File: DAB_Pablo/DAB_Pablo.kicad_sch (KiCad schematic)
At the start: 27 parts, among them U1 UCC21710QDWQ1

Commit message: Se completa Primary Side Half-Bridge 1
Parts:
- added C155, C157, C325, C326: 10uF/50V, Capacitor_SMD:C_1206_3216Metric, symbol Device:C
- added C156, C158: 0.1uF/50V, Capacitor_SMD:C_0201_0603Metric, symbol Device:C
- added C159, C160, C165, C167: 100nF, Capacitor_SMD:C_0201_0603Metric, symbol Device:C
- added C161, C162, C163, C164: 330pF, Capacitor_SMD:C_0201_0603Metric, symbol Device:C
- added C166, C168: 2.2uF/50V, Capacitor_SMD:C_1206_3216Metric, symbol Device:C
- added C171, C176, C181: 0.1uF/50V, Capacitor_SMD:C_1206_3216Metric, symbol Device:C
- added C172: 3.3uF/50V, Capacitor_SMD:C_1206_3216Metric, symbol Device:C
- added C177: 1uF/100V, Capacitor_SMD:C_1206_3216Metric, symbol Device:C
- added C180, C184, C190, C191, C192: 100pF/50V, Capacitor_SMD:C_0201_0603Metric, symbol Device:C
- added C182: 0.47uF/50V, Capacitor_SMD:C_1206_3216Metric, symbol Device:C
- added C189: 330pF/50V, Capacitor_SMD:C_0201_0603Metric, symbol Device:C
- added D15: 1200 V 1A, Diode_SMD:D_SMA, symbol Device:D
- added D17, D20: LED, LED_SMD:LED_0201_0603Metric, symbol Device:LED
- added R144, R150: 0, Resistor_SMD:R_0201_0603Metric, symbol Device:R
- added R154: 15k, Resistor_SMD:R_0201_0603Metric, symbol Device:R
- added R155: 18k, Resistor_SMD:R_0201_0603Metric, symbol Device:R
- added R171: 2k, Resistor_SMD:R_0201_0603Metric, symbol Device:R
- added R183, R4: 1.0k, Resistor_SMD:R_0201_0603Metric, symbol Device:R
- added R185, R187: 100k, Resistor_SMD:R_0201_0603Metric, symbol Device:R
- added R186, R190, R24, R25: 10k, Resistor_SMD:R_0201_0603Metric, symbol Device:R
- added R188, R191: 107k, Resistor_SMD:R_0201_0603Metric, symbol Device:R
- added R189, R192: 30k, Resistor_SMD:R_0201_0603Metric, symbol Device:R
- added R196, R198: 16.2k, Resistor_SMD:R_0201_0603Metric, symbol Device:R
- added R197, R199: 49.9k, Resistor_SMD:R_0201_0603Metric, symbol Device:R
- added R201, R203, R214: 100, Resistor_SMD:R_0201_0603Metric, symbol Device:R
- added R215, R218: 2, Resistor_SMD:R_1206_3216Metric, symbol Device:R
- added R90, R93: 3.6k, Resistor_SMD:R_0201_0603Metric, symbol Device:R
- added U14, U24: UCC14141QDWNRQ1, SSOP36_DWN_TEX, symbol UCC14141QDWNRQ1:UCC14141QDWNRQ1
- added U30: UCC21710QDWQ1, SOIC16_DW_TEX, symbol UCC21710:UCC21710QDWQ1
- renumbered U1 to U29
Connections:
- net +15V_TOP1: now also C165.2, C166.2, C167.2, C168.2, R154.2, R188.2, R191.2, R24.2, R25.2, U14.28 (VDD), U14.29 (VDD), U24.28 (VDD), U24.29 (VDD), U30.5 (VDD)
- net -4V_TOP1: now also C161.1, C162.1, C163.1, C164.1, C165.1, C166.1, C167.1, C168.1, D17.1 (K), D20.1 (K), R196.1, R197.1, R198.1, R199.1, U14.19 (VEE), U14.20 (VEE), U14.21 (VEE), U14.22 (VEE), U14.23 (VEE), U14.24 (VEE), U14.25 (VEE), U14.26 (VEE), U14.27 (VEE), U14.30 (VEE), U14.31 (VEE), U14.35 (VEEA), U14.36 (VEE), U24.19 (VEE), U24.20 (VEE), U24.21 (VEE), U24.22 (VEE), U24.23 (VEE), U24.24 (VEE), U24.25 (VEE), U24.26 (VEE), U24.27 (VEE), U24.30 (VEE), U24.31 (VEE), U24.35 (VEEA), U24.36 (VEE)
- net GND1: now also C155.1, C156.1, C157.1, C158.1, C159.1, C160.1, C180.1, C184.1, C190.1, C191.1, C192.1, C325.1, C326.1, R90.1, R93.1, U14.1 (GNDP), U14.10 (GNDP), U14.11 (GNDP), U14.12 (GNDP), U14.13 (GNDP), U14.14 (GNDP), U14.15 (GNDP), U14.16 (GNDP), U14.17 (GNDP), U14.18 (GNDP), U14.2 (GNDP), U14.5 (GNDP), U14.8 (GNDP), U14.9 (GNDP), U24.1 (GNDP), U24.10 (GNDP), U24.11 (GNDP), U24.12 (GNDP), U24.13 (GNDP), U24.14 (GNDP), U24.15 (GNDP), U24.16 (GNDP), U24.17 (GNDP), U24.18 (GNDP), U24.2 (GNDP), U24.5 (GNDP), U24.8 (GNDP), U24.9 (GNDP), U30.9 (GND)
- net GND_TOP1: now also C189.1, R171.1, R183.1, R189.2, R192.2, R4.1
- net PWM1A_1: now also R201.1
- net PWM1B_1: now also R203.1
- net RDY: now also R144.1
- net TMP_HB1_P: now also U30.16 (APWM)
- net /DESAT_PRI: now also R150.1
- net /RST: now also R214.1
- net -3V3_D renamed 3V3_D
- net 3V3_D: now also C191.2, C192.2, R185.1, R187.1, U30.15 (VCC)
- new net: C189.2, R155.1, R171.2, U30.2 (OC)
- new net: C161.2, R188.1, R196.2, U14.34 (FBVDD)
- new net: R185.2, U14.3 (*PG)
- new net: R183.2, U14.32 (RLIM)
- new net: C162.2, R189.1, R197.2, U14.33 (FBVEE)
- new net: C159.2, R186.1, R90.2, U14.4 (ENA)
- new net: C164.2, R192.1, R199.2, U24.33 (FBVEE)
- new net: C184.2, R203.2, U30.11 (IN-)
- new net: R144.2, U30.12 (RDY)
- new net: C160.2, R190.1, R93.2, U24.4 (ENA)
- new net: C190.2, R214.2, U30.14 (*RST/EN)
- new net: C163.2, R191.1, R198.2, U24.34 (FBVDD)
- new net: R187.2, U24.3 (*PG)
- new net: R4.2, U24.32 (RLIM)
- new net: D15.2 (A), R154.1, R155.2
- new net: D17.2 (A), R24.1
- new net: C180.2, R201.2, U30.10 (IN+)
- new net: R150.2, U30.13 (*FLT)
- new net: R218.1, U30.4 (OUTH)
- new net: R215.1, U30.6 (OUTL)
- new net: D20.2 (A), R25.1
- new net +15V_BOT1: C176.1, C177.1, C181.1, C182.1
- new net -4V_BOT1: C171.2, C172.2, C176.2, C177.2, U30.8 (VEE)
- new net 12V: C155.2, C156.2, C157.2, C158.2, C325.2, C326.2, R186.2, R190.2, U14.6 (VIN), U14.7 (VIN), U24.6 (VIN), U24.7 (VIN)
- new net D1L_P: D15.1 (K)
- new net G1L_P: R215.2, R218.2, U30.7 (CLMPI)
- new net GND_BOT1: C171.1, C172.1, C181.2, C182.2, U30.1 (AIN), U30.3 (COM)
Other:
- note added: "Primary Side Half-Bridge 1"
- title: (none) -> 10KW DC-DC CONVERTER
- moved on the sheet: C1, C169, C170, C173, C174, C175, C178, C179, C183, C185, C188, C2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

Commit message: Se completa Primary Side Half-Bridge 2
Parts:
- removed C1, C175, C180, C183, C184, C185, C190, C191, C192, C2: 100pF/50V, Capacitor_SMD:C_0201_0603Metric, symbol Device:C
- removed C155, C157, C325, C326: 10uF/50V, Capacitor_SMD:C_1206_3216Metric, symbol Device:C
- removed C156, C158: 0.1uF/50V, Capacitor_SMD:C_0201_0603Metric, symbol Device:C
- removed C159, C160, C165, C167, C78: 100nF, Capacitor_SMD:C_0201_0603Metric, symbol Device:C
- removed C161, C162, C163, C164: 330pF, Capacitor_SMD:C_0201_0603Metric, symbol Device:C
- removed C166, C168: 2.2uF/50V, Capacitor_SMD:C_1206_3216Metric, symbol Device:C
- removed C169, C171, C173, C176, C178, C181: 0.1uF/50V, Capacitor_SMD:C_1206_3216Metric, symbol Device:C
- removed C170, C172: 3.3uF/50V, Capacitor_SMD:C_1206_3216Metric, symbol Device:C
- removed C174, C177: 1uF/100V, Capacitor_SMD:C_1206_3216Metric, symbol Device:C
- removed C179, C182: 0.47uF/50V, Capacitor_SMD:C_1206_3216Metric, symbol Device:C
- removed C188, C189: 330pF/50V, Capacitor_SMD:C_0201_0603Metric, symbol Device:C
- removed D14, D15: 1200 V 1A, Diode_SMD:D_SMA, symbol Device:D
- removed D17, D20: LED, LED_SMD:LED_0201_0603Metric, symbol Device:LED
- removed R144, R147, R150, R85: 0, Resistor_SMD:R_0201_0603Metric, symbol Device:R
- removed R154, R208: 15k, Resistor_SMD:R_0201_0603Metric, symbol Device:R
- removed R155, R217: 18k, Resistor_SMD:R_0201_0603Metric, symbol Device:R
- removed R16: 10, Resistor_SMD:R_0201_0603Metric, symbol Device:R
- removed R171, R223: 2k, Resistor_SMD:R_0201_0603Metric, symbol Device:R
- removed R183, R4: 1.0k, Resistor_SMD:R_0201_0603Metric, symbol Device:R
- removed R185, R187: 100k, Resistor_SMD:R_0201_0603Metric, symbol Device:R
- removed R186, R190, R24, R25: 10k, Resistor_SMD:R_0201_0603Metric, symbol Device:R
- removed R188, R191: 107k, Resistor_SMD:R_0201_0603Metric, symbol Device:R
- removed R189, R192: 30k, Resistor_SMD:R_0201_0603Metric, symbol Device:R
- removed R196, R198: 16.2k, Resistor_SMD:R_0201_0603Metric, symbol Device:R
- removed R197, R199: 49.9k, Resistor_SMD:R_0201_0603Metric, symbol Device:R
- removed R200, R201, R202, R203, R214, R220: 100, Resistor_SMD:R_0201_0603Metric, symbol Device:R
- removed R209, R215, R216, R218: 2, Resistor_SMD:R_1206_3216Metric, symbol Device:R
- removed R90, R93: 3.6k, Resistor_SMD:R_0201_0603Metric, symbol Device:R
- removed RT1: TMP6131DECR, symbol Device:Thermistor_PTC
- removed U14, U24: UCC14141QDWNRQ1, SSOP36_DWN_TEX, symbol UCC14141QDWNRQ1:UCC14141QDWNRQ1
- removed U29, U30: UCC21710QDWQ1, SOIC16_DW_TEX, symbol UCC21710:UCC21710QDWQ1
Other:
- added sheet Primary Side Half-Bridge 1 (untitled.kicad_sch)
- added sheet Primary Side Half-Bridge 2 (Primary Side Half-Bridge 1.kicad_sch)
- note removed: "Primary Side Half-Bridge 1"

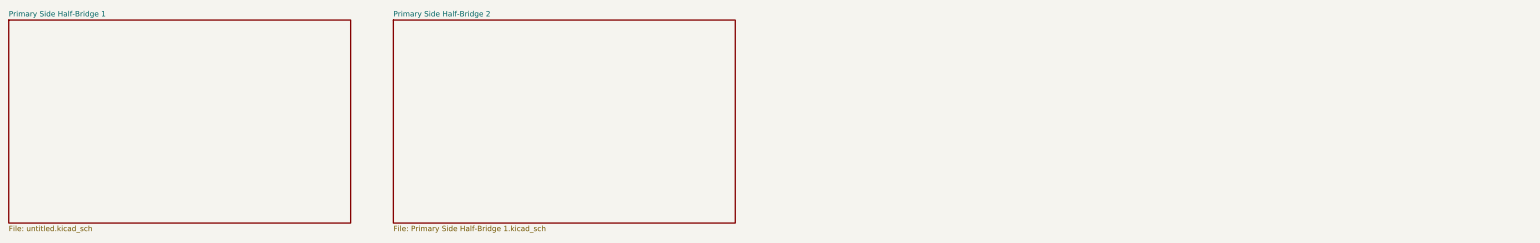
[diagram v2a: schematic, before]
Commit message: Se finaliza todos los half-bridge
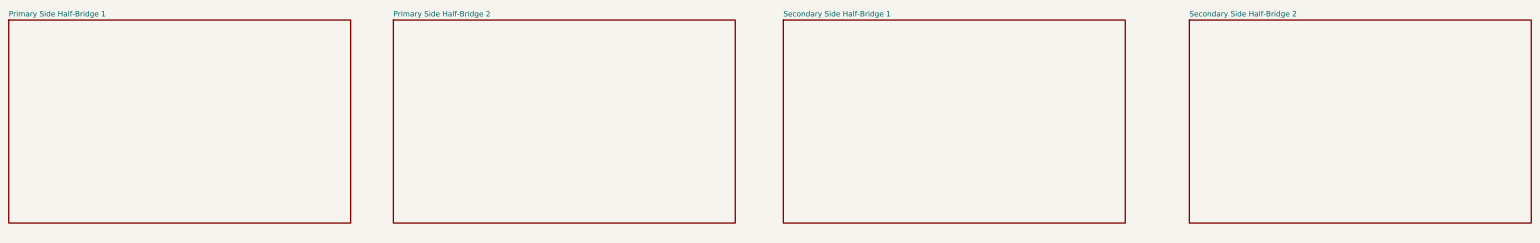
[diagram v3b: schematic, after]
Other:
- added sheet Secondary Side Half-Bridge 1 (Secondary Side Half-Bridge 1.kicad_sch)
- added sheet Secondary Side Half-Bridge 2 (Secondary Side Half-Bridge 2.kicad_sch)
- sheet Primary Side Half-Bridge 2: file Primary Side Half-Bridge 1.kicad_sch -> Primary Side Half-Bridge 2.kicad_sch
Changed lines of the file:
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@@
 				)
 				(justify left top)
+				(hide yes)
 			)
 		)
@@
 			)
 		)
-		(property "Sheetfile" "Primary Side Half-Bridge 1.kicad_sch"
+		(property "Sheetfile" "Primary Side Half-Bridge 2.kicad_sch"
 			(at 119.38 74.2446 0)
 			(effects
@@
 				)
 				(justify left top)
+				(hide yes)
 			)
 		)
@@
 				)
 			)
+		)
+	)
+	(sheet
+		(at 212.09 25.4)
+		(size 81.28 48.26)
+		(fields_autoplaced yes)
+		(stroke
+			(width 0.1524)
+			(type solid)
+		)
+		(fill
+			(color 0 0 0 0.0000)
+		)
+		(property "Sheetname" "Secondary Side Half-Bridge 1"
+			(at 212.09 24.6884 0)
+			(effects
+				(font
+					(size 1.27 1.27)
+				)
+				(justify left bottom)
+			)
+		)
+		(property "Sheetfile" "Secondary Side Half-Bridge 1.kicad_sch"
+			(at 212.09 74.2446 0)
+			(effects
+				(font
+					(size 1.27 1.27)
+				)
+				(justify left top)
+				(hide yes)
+			)
+		)
+		(instances
+			(project "DAB_Pablo"
+				(path "/f6cfbc7d-296b-4fcc-b130-a6ec96f5f92b"
+					(page "4")
+				)
+			)
+		)
+	)
+	(sheet
+		(at 308.61 25.4)
+		(size 81.28 48.26)
+		(fields_autoplaced yes)
+		(stroke
+			(width 0.1524)
+			(type solid)
+		)
+		(fill
+			(color 0 0 0 0.0000)
+		)
+		(property "Sheetname" "Secondary Side Half-Bridge 2"
+			(at 308.61 24.6884 0)
+			(effects
+				(font
+					(size 1.27 1.27)
+				)
+				(justify left bottom)
+			)
+		)
+		(property "Sheetfile" "Secondary Side Half-Bridge 2.kicad_sch"
+			(at 308.61 74.2446 0)
+			(effects
+				(font
+					(size 1.27 1.27)
+				)
+				(justify left top)
+				(hide yes)
+			)
+		)
+		(instances
+			(project "DAB_Pablo"
+				(path "/f6cfbc7d-296b-4fcc-b130-a6ec96f5f92b"
+					(page "5")
+				)
+			)
